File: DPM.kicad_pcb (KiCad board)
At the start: 2 copper layers, 95.9 x 90.2 mm, 43 parts, among them J1 Conn_02x12_Odd_Even, J2 Conn_02x05_Odd_Even, U1 74LS251, U2 74LVC2G74, U25 74LS85, U28 74LS85, U3 ADG333A, U31 74LS85, U4 MCP23017_SP, U5 ADG333A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

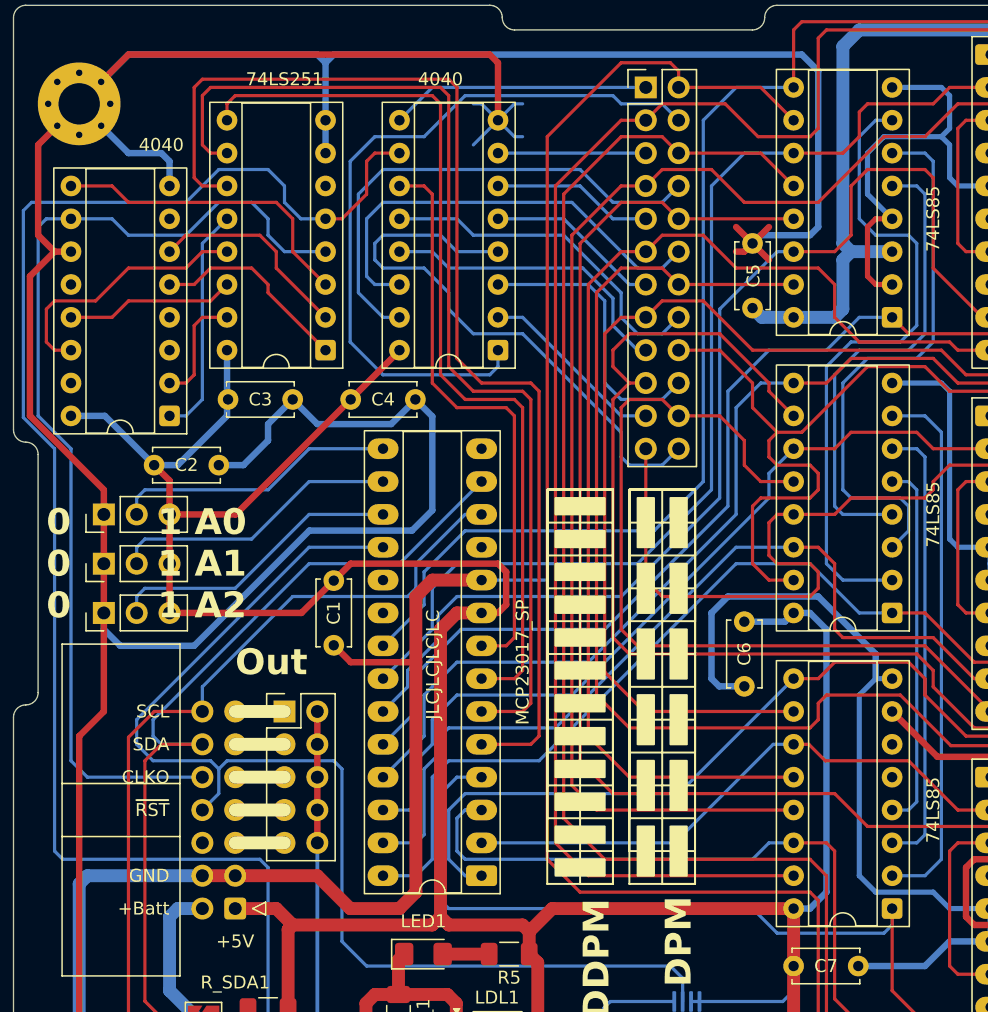
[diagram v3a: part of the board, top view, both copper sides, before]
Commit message: Modification : PinOut des ports GPIOA et GPIOB
git-svn-id: file:///D%5C00%20-%20Dev%20&%20Calculs%5CRepoTortoiseSVN_PCB%5CD-DPM/trunk@24 f29d8339-a183-0348-962e-9e4594cf8312
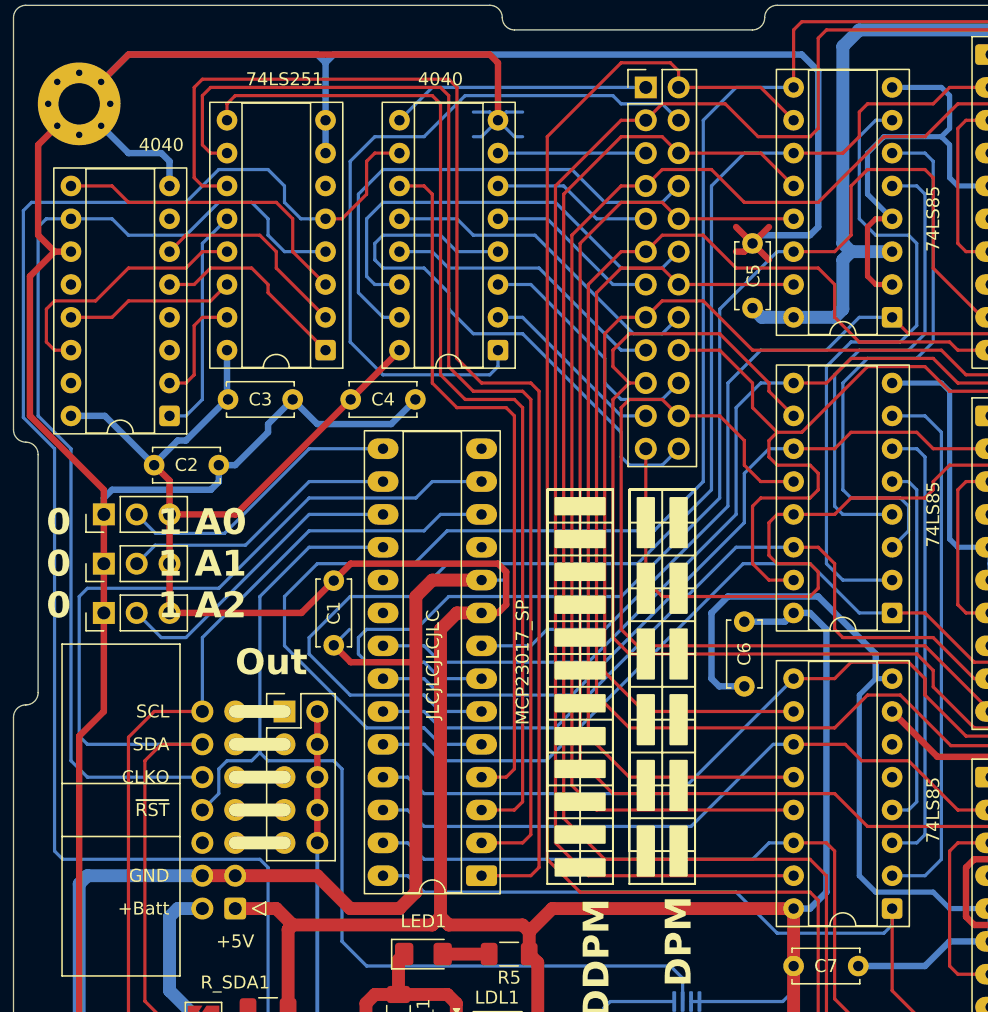
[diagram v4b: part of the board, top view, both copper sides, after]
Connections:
- U4 pad 1: /A8 -> PreScaler0
- U4 pad 2: /A9 -> PreScaler1
- U4 pad 21: /A0 -> /A4
- U4 pad 22: /A1 -> /A5
- U4 pad 23: /A2 -> /A6
- U4 pad 24: /A3 -> /A7
- U4 pad 25: /A4 -> /A8
- U4 pad 26: /A5 -> /A9
- U4 pad 27: /A6 -> /A10
- U4 pad 28: /A7 -> /A11
- U4 pad 3: /A10 -> PreScaler2
- U4 pad 4: /A11 -> ~{CntEN}
- U4 pad 5: PreScaler0 -> /A0
- U4 pad 6: PreScaler1 -> /A1
- U4 pad 7: PreScaler2 -> /A2
- U4 pad 8: ~{CntEN} -> /A3
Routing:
- net Ground: track 792.6 -> 765.7 mm
- net /A0: track 105.7 -> 132.5 mm
- net /A1: track 82.7 -> 101.7 mm
- net SDA: track 66.2 -> 83.2 mm
- net /A3: track 76.2 -> 64.1 mm
- net PreScaler0: track 90.4 -> 100.5 mm
- net ~{CntEN}: track 44.8 -> 54.9 mm
- net PreScaler2: track 70.4 -> 80.6 mm
- net PreScaler1: track 81.5 -> 91.6 mm
- net ~{Reset}: track 90.0 -> 80.1 mm
- net /A2: track 85.8 -> 95.1 mm
- net /A9: track 44.6 -> 52.3 mm
- net /A6: track 67.4 -> 60.5 mm
- net /A7: track 72.0 -> 65.1 mm
- net /A11: track 72.6 -> 65.9 mm
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
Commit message: Création modélisations sous Digital Correction routage des R SDA/SCL Ajout des screenshots de la carte
git-svn-id: file:///D%5C00%20-%20Dev%20&%20Calculs%5CRepoTortoiseSVN_PCB%5CD-DPM/trunk@25 f29d8339-a183-0348-962e-9e4594cf8312
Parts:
- removed Pad_SCL1, Pad_SDA1: SolderJumper_2_Open, Jumper:SolderJumper-2_P1.3mm_Open_TrianglePad1.0x1.5mm
- R_SCL1, R_SDA1: footprint Resistor_SMD:R_1210_3225Metric_Pad1.30x2.65mm_HandSolder -> Resistor_THT:R_Axial_DIN0207_L6.3mm_D2.5mm_P10.16mm_Horizontal
- moved R_SCL1 8.91 mm to (52.1, 125.7)
- moved R_SDA1 8.91 mm to (52.1, 121.9)
- moved J_VIN_0 0.68 mm to (66.0, 128.3)
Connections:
- R_SCL1 pad 1: Net-(Pad_SCL1-A) -> SCL
- R_SDA1 pad 1: Net-(Pad_SDA1-A) -> SDA
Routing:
- net /Clock_loc: track 155.3 -> 150.5 mm
- net SDA: track 83.2 -> 78.8 mm
- net SCL: track 66.2 -> 63.3 mm
- net Net-(ByPass_2G74-B): track 52.8 -> 49.8 mm
- net /CNT_A3: track 99.4 -> 102.2 mm
- net Net-(Pad_SCL1-A): track 2.80 -> 0.00 mm
- net Net-(Pad_SDA1-A): track 2.71 -> 0.00 mm
- net Ground: track 765.7 -> 763.5 mm
- net Net-(U5-D3): track 22.1 -> 24.0 mm
- net VBatt: track 27.6 -> 26.2 mm
- net /A8: track 65.6 -> 66.3 mm
- net +5V: track 424.3 -> 423.8 mm
